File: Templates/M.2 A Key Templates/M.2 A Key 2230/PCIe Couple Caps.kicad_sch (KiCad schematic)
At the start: 2 parts

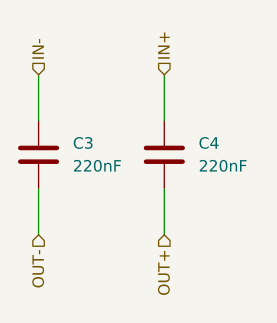
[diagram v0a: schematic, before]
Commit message: Updated PCIe Symbols
fixed pins on all PCIe Symbols input and output are the perspective of the card.
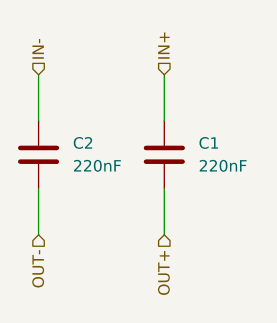
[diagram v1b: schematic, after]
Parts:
- renumbered C4 to C1, C3 to C2
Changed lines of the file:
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@@
 		(dnp no)
 		(fields_autoplaced yes)
-		(property "Reference" "C?"
+		(property "Reference" "C2"
 			(at 133.35 99.0599 0)
 			(effects
@@
 		(dnp no)
 		(fields_autoplaced yes)
-		(property "Reference" "C?"
+		(property "Reference" "C1"
 			(at 147.32 99.0599 0)
 			(effects
